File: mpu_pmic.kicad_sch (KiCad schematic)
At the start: 49 parts, among them U501 STPMIC1DPQR

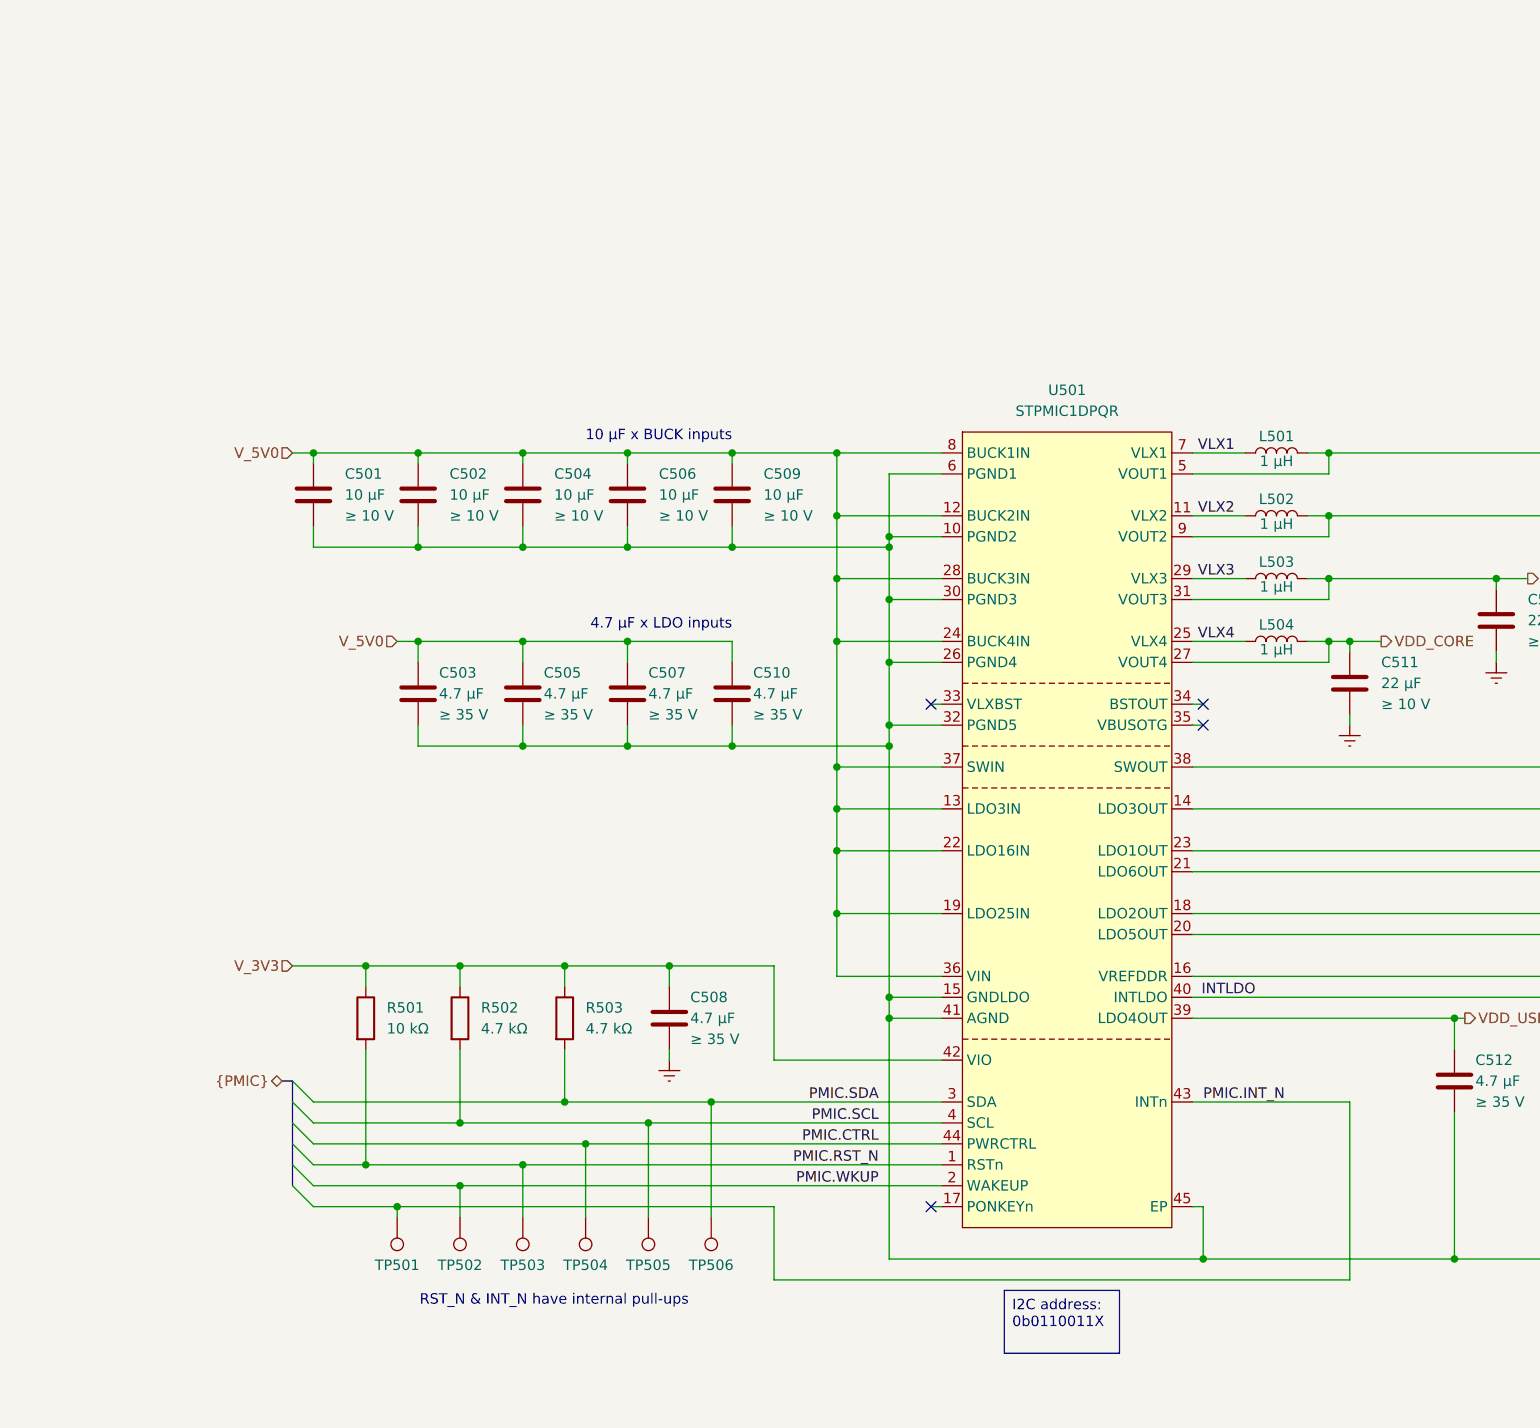
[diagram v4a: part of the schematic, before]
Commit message: Add series termination, refactor schematics
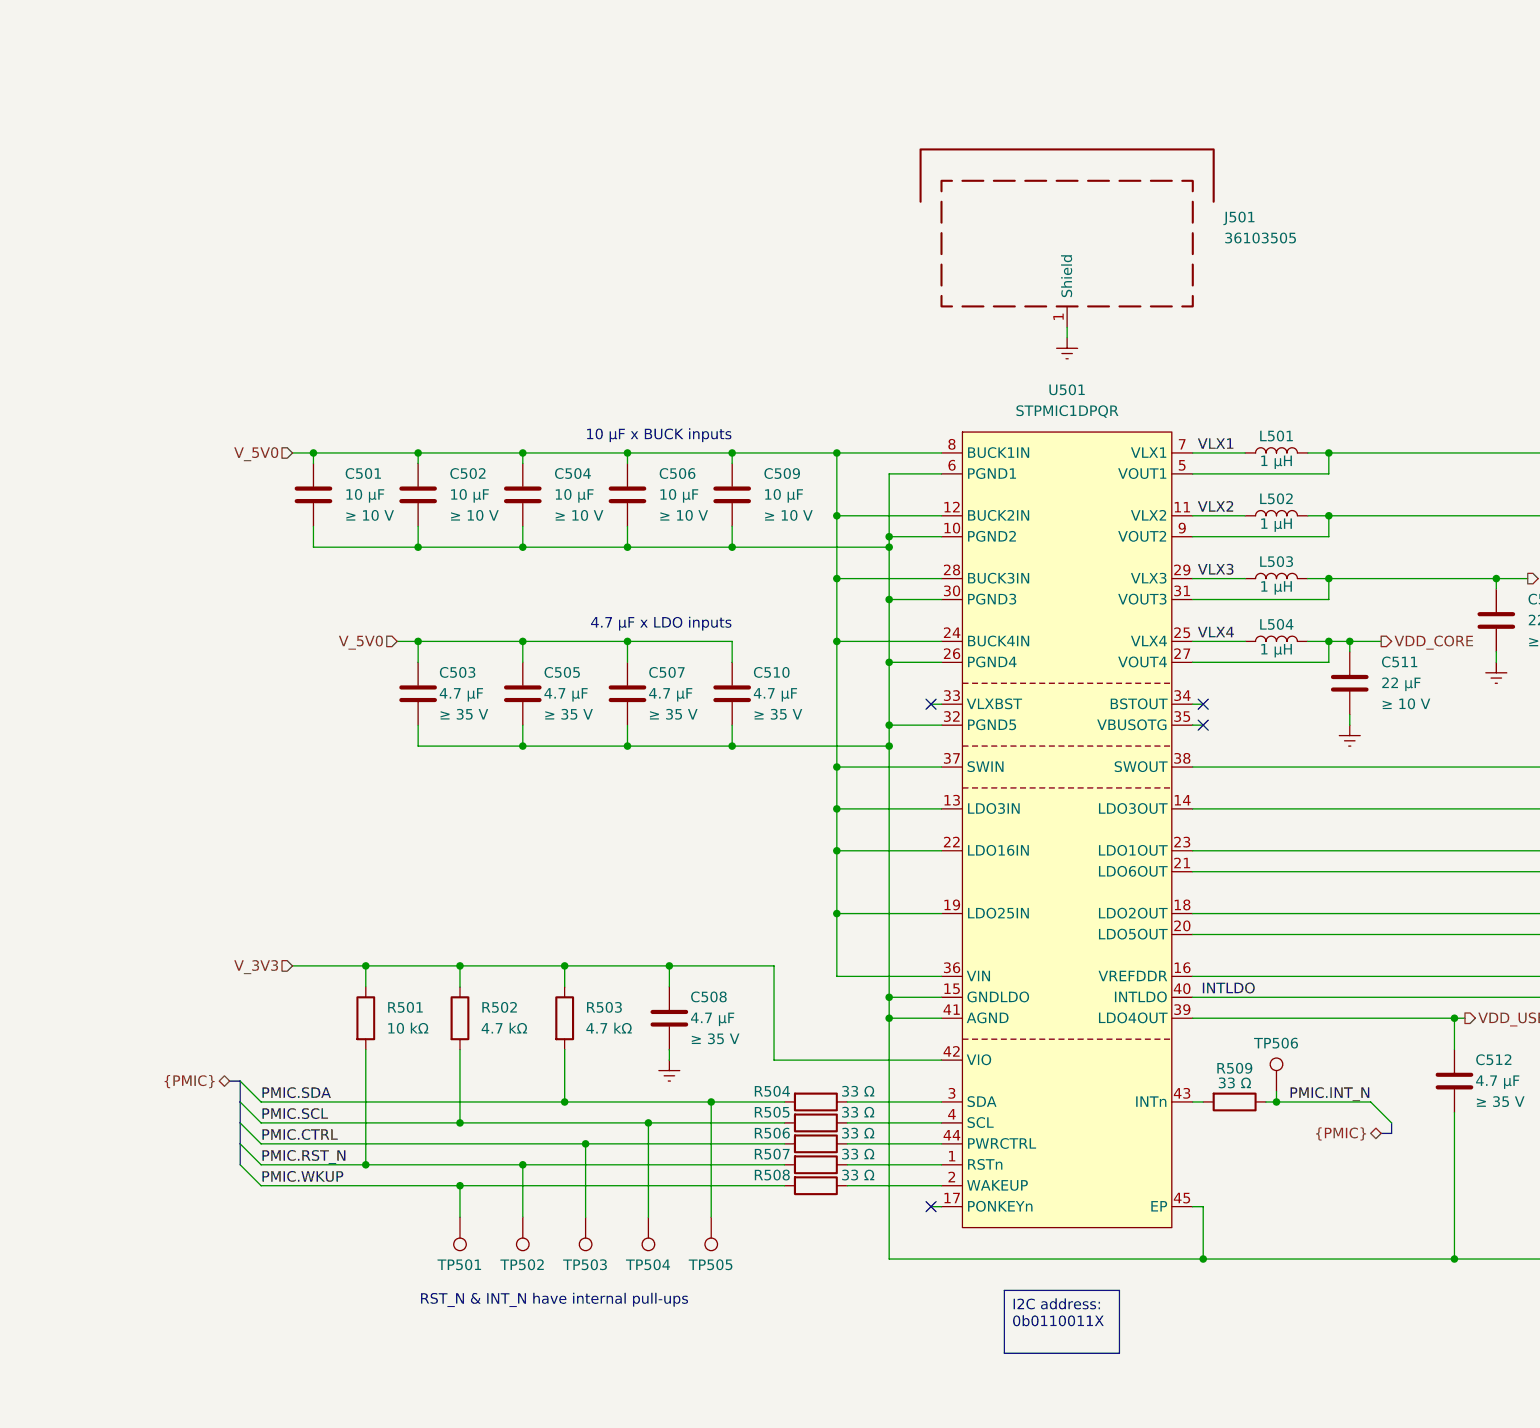
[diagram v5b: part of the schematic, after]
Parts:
- added J501: 36103505, symbol Device:RFShield_TwoPieces
- added R504, R505, R506, R507, R508, R509: 33 Ω, perfect_footprints:R_0402_1005Metric, symbol Device:R
- renumbered TP502 to TP501, TP503 to TP502, TP504 to TP503, TP505 to TP504, TP506 to TP505, TP501 to TP506
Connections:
- net GND: now also J501.1 (Shield)
- net PMIC.CTRL: now also R506.2; no longer U501.44 (PWRCTRL)
- net PMIC.INT_N: now also R509.1; no longer U501.43 (INTn)
- net PMIC.RST_N: now also R507.2; no longer U501.1 (RSTn)
- net PMIC.SCL: now also R505.2; no longer U501.4 (SCL)
- net PMIC.SDA: now also R504.2; no longer U501.3 (SDA)
- net PMIC.WKUP: now also R508.2; no longer U501.2 (WAKEUP)
- new net: R507.1, U501.1 (RSTn)
- new net: R508.1, U501.2 (WAKEUP)
- new net: R504.1, U501.3 (SDA)
- new net: R505.1, U501.4 (SCL)
- new net: R509.2, U501.43 (INTn)
- new net: R506.1, U501.44 (PWRCTRL)
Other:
- moved on the sheet: TP506

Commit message: Refactor symbol properties
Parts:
- C501, C502, C504, C506, C509, C511, C513, C515, C517: DigiKey Part Number 490-13248-1-ND -> (none)
- C503, C505, C507, C508, C510, C512, C514, C516, C518, C519, C520, C521, C522, C523: DigiKey Part Number 490-7205-1-ND -> (none)
- R501, R504, R505, R506, R507, R508, R509: DigiKey Part Number 732-560112110020CT-ND -> (none)
- R502, R503: DigiKey Part Number 732-560112110019CT-ND -> (none)

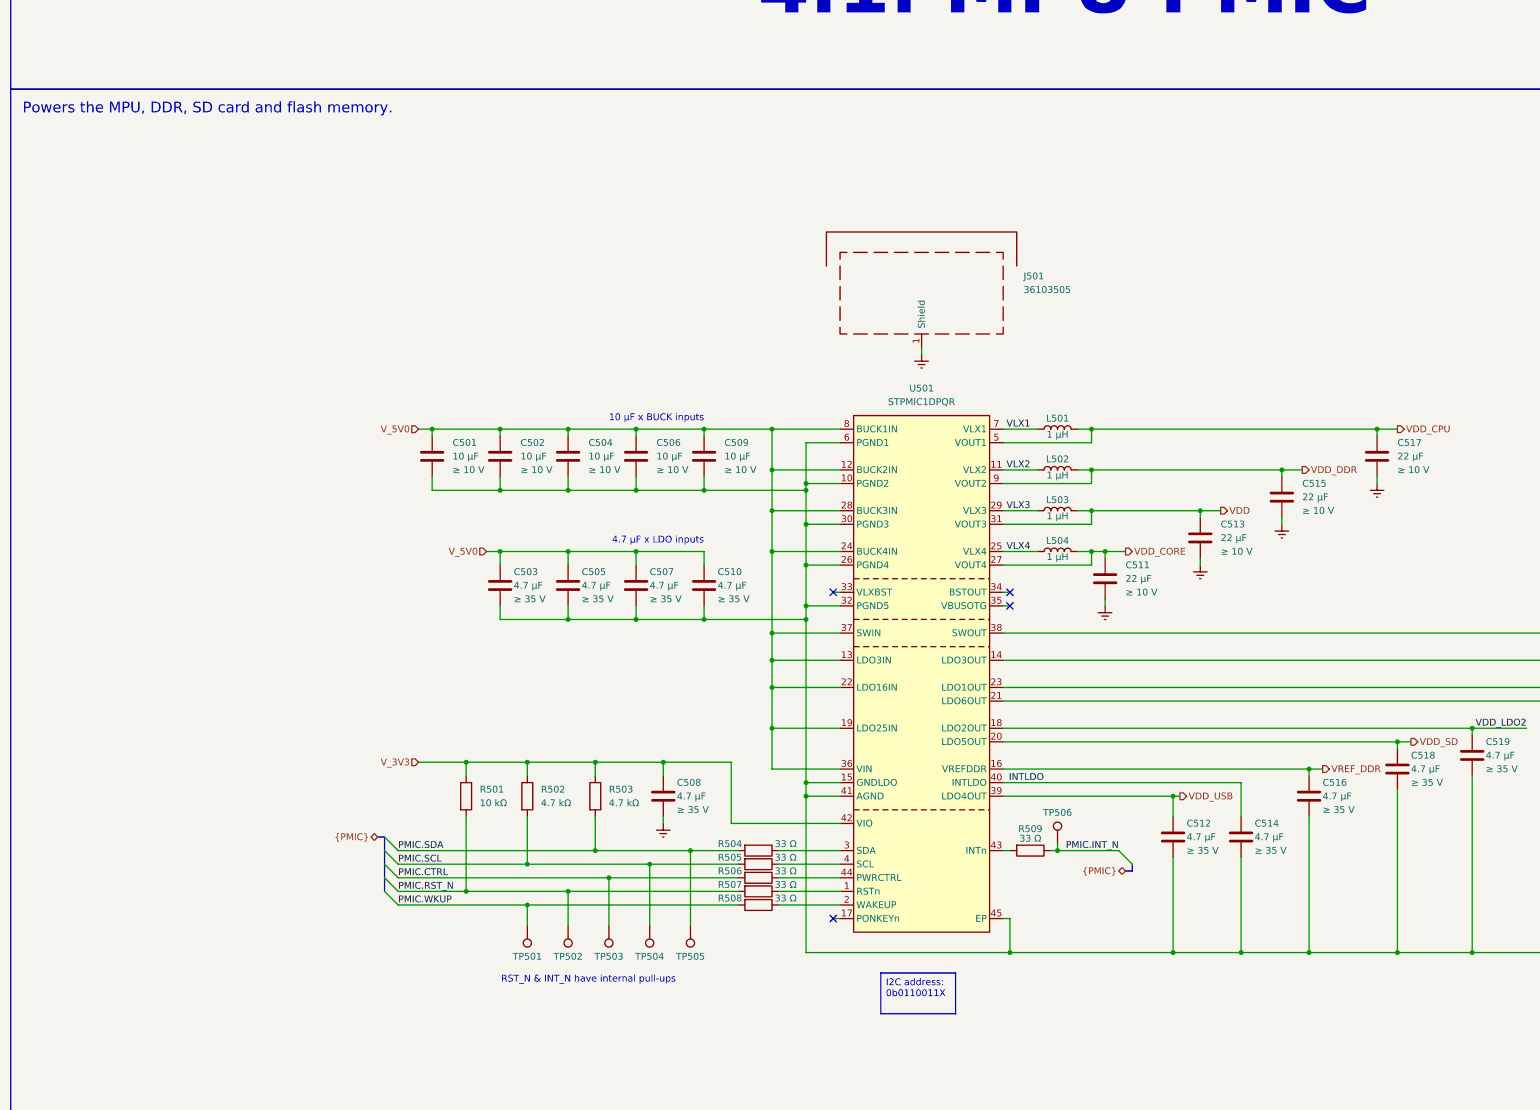
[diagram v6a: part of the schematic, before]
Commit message: Refactor MPU and USB
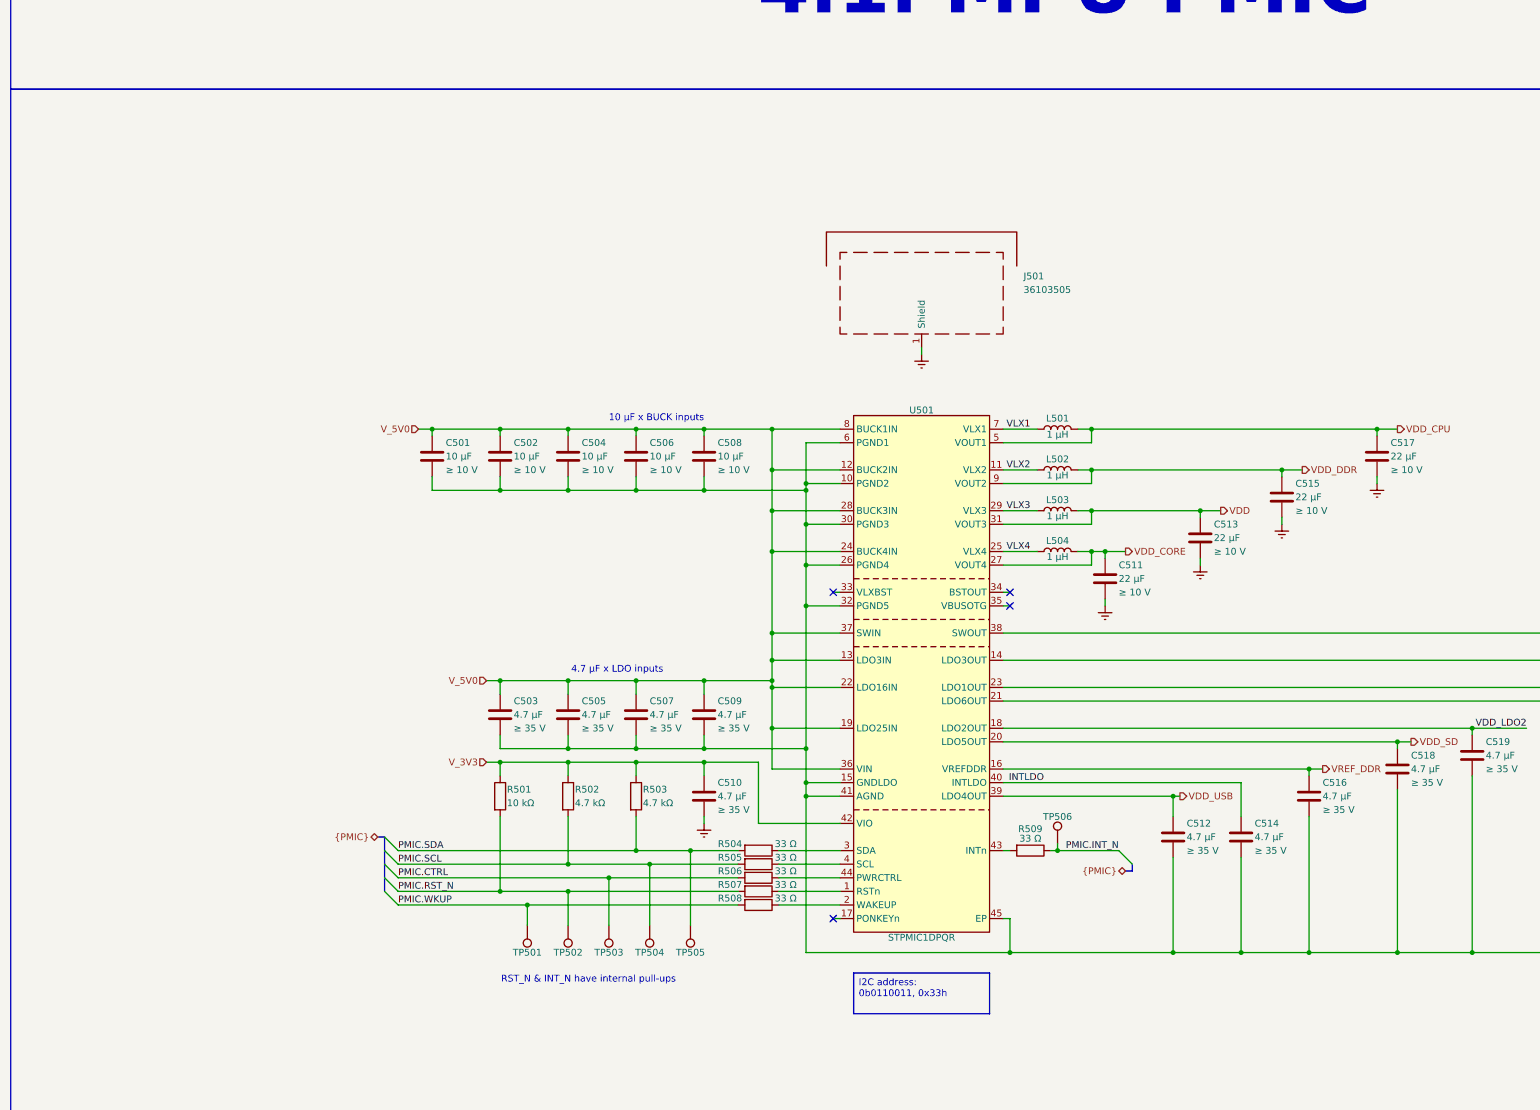
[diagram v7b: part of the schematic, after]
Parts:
- renumbered C509 to C508, C510 to C509, C508 to C510
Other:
- moved on the sheet: C503, C505, C507, C509, C510, R501, R502, R503

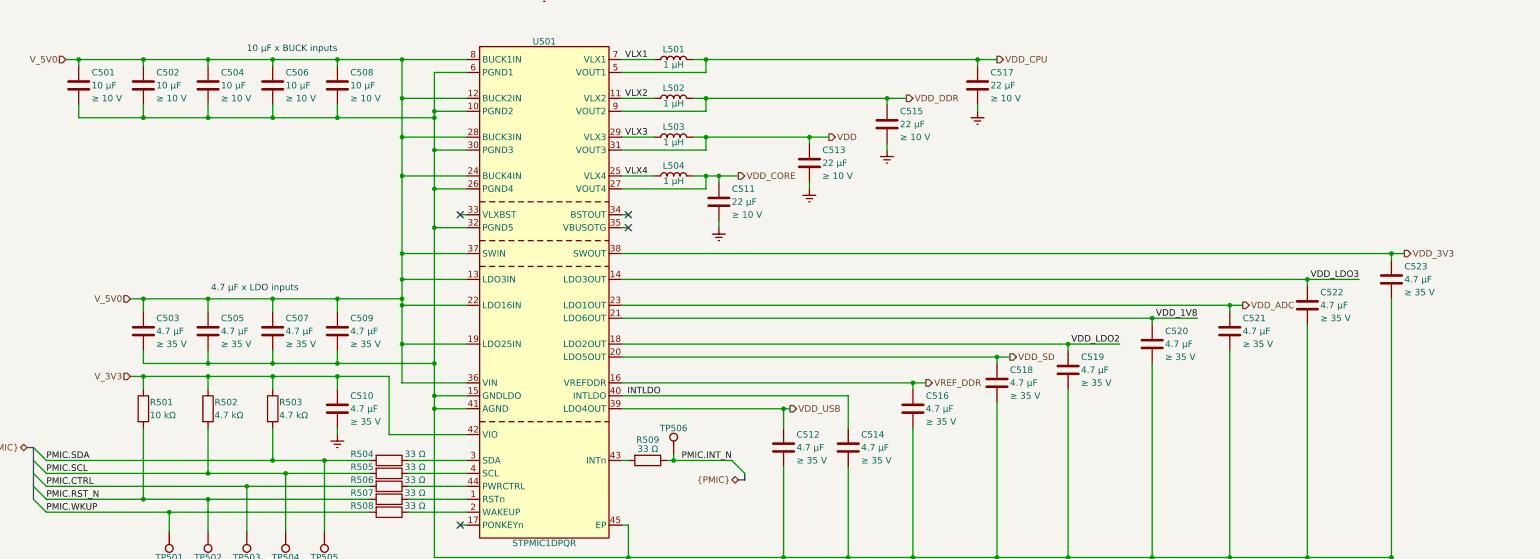
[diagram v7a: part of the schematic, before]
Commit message: Fix component values
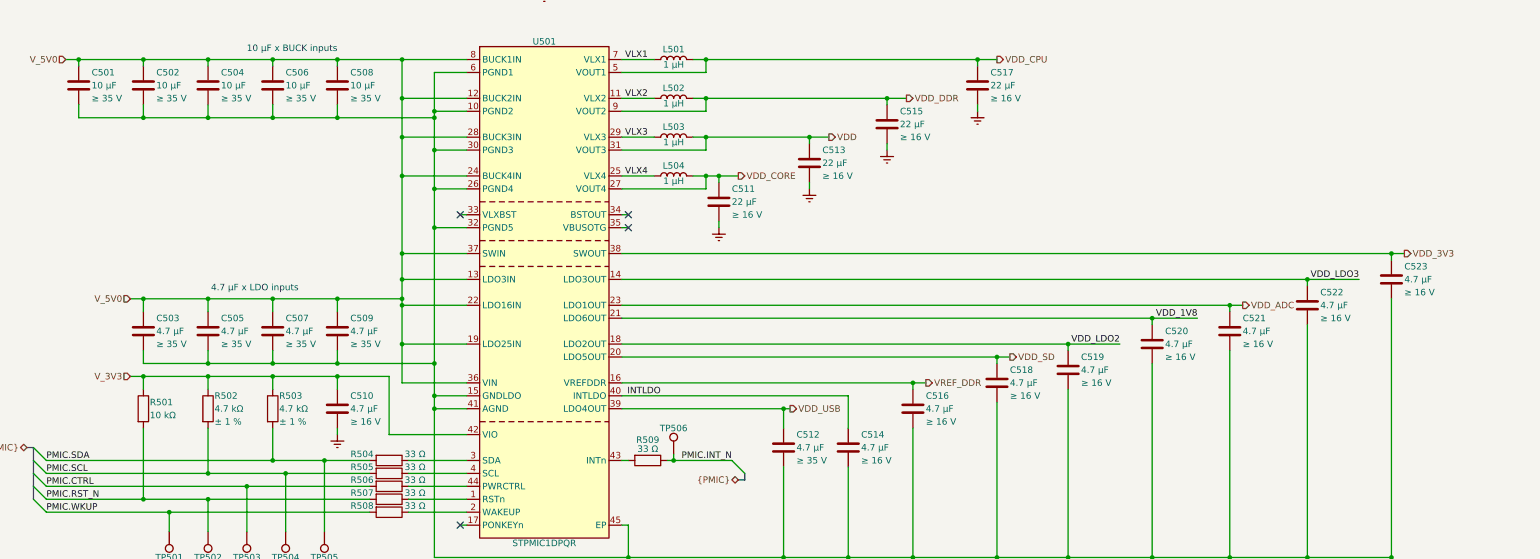
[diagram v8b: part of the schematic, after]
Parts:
- C501, C502, C504, C506, C508: Voltage rating ≥ 10 V -> ≥ 35 V
- C510, C514, C516, C518, C519, C520, C521, C522, C523: Voltage rating ≥ 35 V -> ≥ 16 V
- C511, C513, C515, C517: Voltage rating ≥ 10 V -> ≥ 16 V
- R502, R503: MPN 560112110019 -> (none); Manufacturer Würth Elektronik -> (none); Tolerance (none) -> ± 1 %
